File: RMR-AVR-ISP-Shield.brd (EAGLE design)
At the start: 68.6 x 53.3 mm, 31 parts, among them IC1 AVR-MEGA-PZIF_SOCKET, J1 AVR_SPI_PRG_6PTH, U1 ARDUINO_SHIELDLABEL, X1 16.00MHz, Y1 16MHz

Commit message: Add files via upload
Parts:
- added C4: 10uF, SparkFun-Capacitors:CPOL-RADIAL-2.5MM-5MM
- moved SW2 10.2 mm to (17.8, 2.54), turned to 0 degrees
- moved R3 5.08 mm to (47.0, 34.3)
- moved R4 2.54 mm to (47.0, 39.4)
- moved R5 2.54 mm to (47.0, 36.8)
- moved JP1 1.80 mm to (0.00, 8.89)
- moved LED1 1.27 mm to (31.8, 36.8)
- moved LED2 1.27 mm to (31.8, 44.5)
- moved LED3 1.27 mm to (19.1, 36.8)
- moved LED4 1.27 mm to (19.1, 44.5)
- turned R6 to 270 degrees
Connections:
- net GND: now also C4.2
- net RES: now also C4.1
- net RX: no longer IC1.3
- net TX: no longer IC1.2
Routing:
- net MISO: track 20.2 -> 74.1 mm
- net MOSI: track 21.7 -> 65.0 mm
- net SCK: track 23.5 -> 64.4 mm
- net SLV_RST: track 62.8 -> 96.0 mm
- net RES: track 25.2 -> 35.4 mm
- net N$6: track 45.4 -> 35.9 mm
- net XTAL1: track 13.8 -> 18.1 mm
- net N$1: track 11.0 -> 7.85 mm
- net TX: track 0.00 -> 2.54 mm
- net RX: track 0.00 -> 2.54 mm
- net VCC: track 115.4 -> 117.5 mm
- net N$5: track 15.5 -> 13.8 mm
- net N$4: track 12.0 -> 10.7 mm
- net N$2: track 12.0 -> 10.7 mm
- net D9: track 12.3 -> 13.5 mm
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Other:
- board text added: "PROG"
- board text removed: "8/24/21"
- board text removed: "PROGRAM"

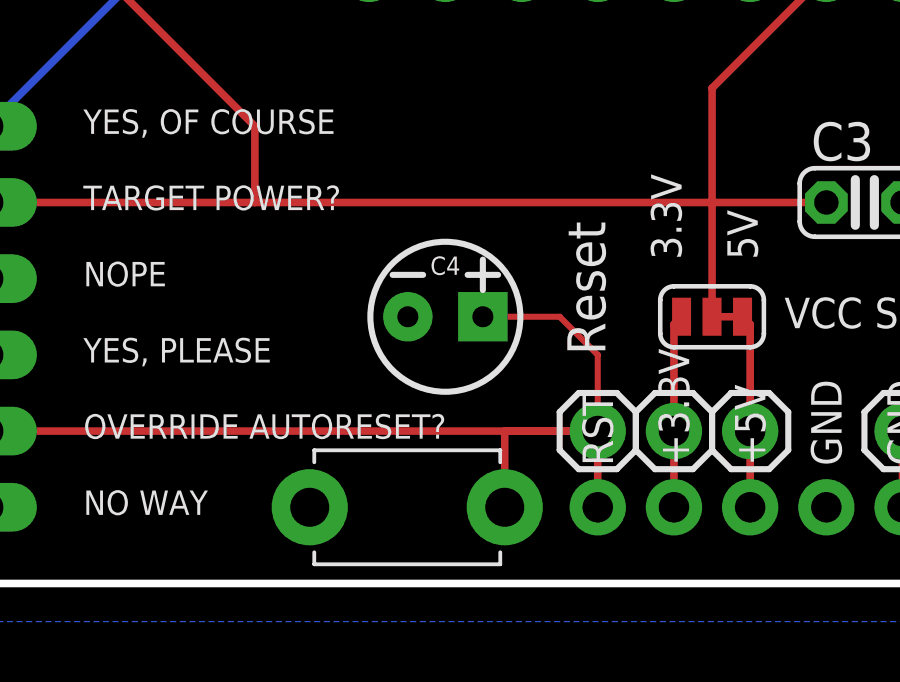
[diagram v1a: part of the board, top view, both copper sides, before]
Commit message: Add files via upload
changed reset capacitor
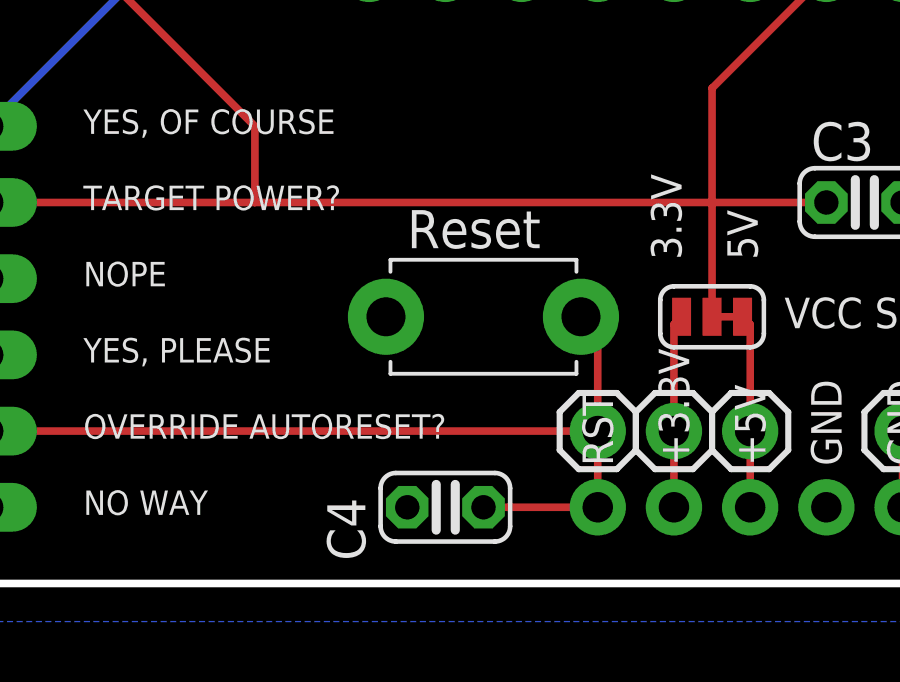
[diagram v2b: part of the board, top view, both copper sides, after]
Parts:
- C4: value 10uF -> 0.1uF; device SparkFun-Capacitors:CPOL-RADIAL-2.5MM-5MM -> adafruit:C025-024X044
- moved SW2 6.84 mm to (20.3, 8.89)
- moved C4 6.35 mm to (19.1, 2.54)
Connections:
- net GND: now also C4.1; no longer C4.2
- net RES: now also C4.2; no longer C4.1
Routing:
- net RES: track 35.4 -> 30.7 mm
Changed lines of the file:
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@@
 <text x="6.985" y="14.986" size="0.8128" layer="21" font="vector" ratio="15">YES, OF COURSE</text>
 <text x="29.464" y="10.795" size="1.016" layer="21" font="vector" ratio="15" rot="R90">5V</text>
-<text x="24.384" y="7.62" size="1.27" layer="21" font="vector" ratio="15" rot="R90">Reset</text>
+<text x="17.78" y="11.176" size="1.27" layer="21" font="vector" ratio="15">Reset</text>
 <text x="52.07" y="23.749" size="1.778" layer="22" font="vector" ratio="15" rot="MR0">RabbitMountainResearch.com</text>
 </plain>
@@
 <attribute name="VALUE" x="53.34" y="46.736" size="0.6096" layer="27" font="vector" ratio="20" align="top-left"/>
 </element>
-<element name="SW2" library="adafruit" library_urn="urn:adsk.eagle:library:420" package="TACT_PANA-EVQ" package3d_urn="urn:adsk.eagle:package:6240957/1" value="" x="17.78" y="2.54" smashed="yes">
-<attribute name="VALUE" x="14.764" y="0.089" size="0.4064" layer="27" ratio="10"/>
-</element>
-<element name="C4" library="SparkFun-Capacitors" library_urn="urn:adsk.eagle:library:510" package="CPOL-RADIAL-2.5MM-5MM" package3d_urn="urn:adsk.eagle:package:37423/1" value="10uF" x="19.05" y="8.89" smashed="yes">
-<attribute name="NAME" x="19.05" y="10.287" size="0.6096" layer="25" font="vector" ratio="20" align="bottom-center"/>
-<attribute name="PROD_ID" value="CAP-08440" x="19.05" y="8.89" size="1.778" layer="27" display="off"/>
-<attribute name="VALUE" x="19.05" y="7.493" size="0.6096" layer="27" font="vector" ratio="20" align="top-center"/>
+<element name="SW2" library="adafruit" library_urn="urn:adsk.eagle:library:420" package="TACT_PANA-EVQ" package3d_urn="urn:adsk.eagle:package:6240957/1" value="" x="20.32" y="8.89" smashed="yes">
+<attribute name="VALUE" x="17.304" y="6.439" size="0.4064" layer="27" ratio="10"/>
+</element>
+<element name="C4" library="adafruit" library_urn="urn:adsk.eagle:library:420" package="C025-024X044" package3d_urn="urn:adsk.eagle:package:6240324/1" value="0.1uF" x="19.05" y="2.54" smashed="yes">
+<attribute name="NAME" x="16.383" y="0.762" size="1.27" layer="25" ratio="10" rot="R90"/>
 </element>
 </elements>
@@
 <vertex x="-10.16" y="54.61"/>
 </polygon>
-<contactref element="C4" pad="2"/>
+<contactref element="C4" pad="1"/>
 </signal>
 <signal name="5V">
@@
 <contactref element="SW2" pad="P$2"/>
 <wire x1="24.13" y1="2.54" x2="24.13" y2="5.08" width="0.254" layer="1"/>
-<wire x1="24.13" y1="5.08" x2="21.03" y2="5.08" width="0.254" layer="1"/>
-<wire x1="21.03" y1="5.08" x2="21.03" y2="2.54" width="0.254" layer="1"/>
 <wire x1="3.81" y1="5.08" x2="24.13" y2="5.08" width="0.254" layer="1"/>
-<contactref element="C4" pad="1"/>
-<wire x1="20.3" y1="8.89" x2="22.86" y2="8.89" width="0.2032" layer="1"/>
-<wire x1="24.13" y1="7.62" x2="22.86" y2="8.89" width="0.2032" layer="1"/>
-<wire x1="24.13" y1="7.62" x2="24.13" y2="5.08" width="0.2032" layer="1"/>
+<contactref element="C4" pad="2"/>
+<wire x1="23.57" y1="8.89" x2="24.13" y2="8.33" width="0.254" layer="1"/>
+<wire x1="24.13" y1="8.33" x2="24.13" y2="5.08" width="0.254" layer="1"/>
+<wire x1="20.32" y1="2.54" x2="24.13" y2="2.54" width="0.254" layer="1"/>
 </signal>
 <signal name="VCC">

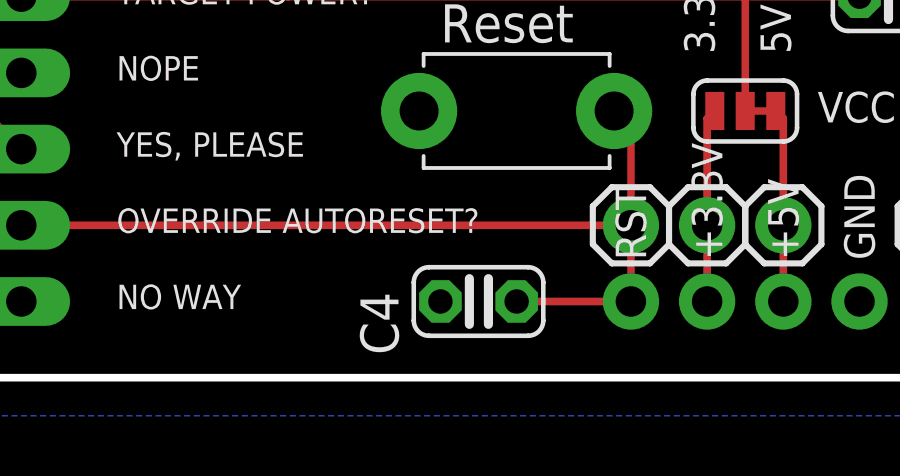
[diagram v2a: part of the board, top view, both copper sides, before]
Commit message: Add files via upload
added jumper to the reset capacitor for UNO / 328p based Arduinos.
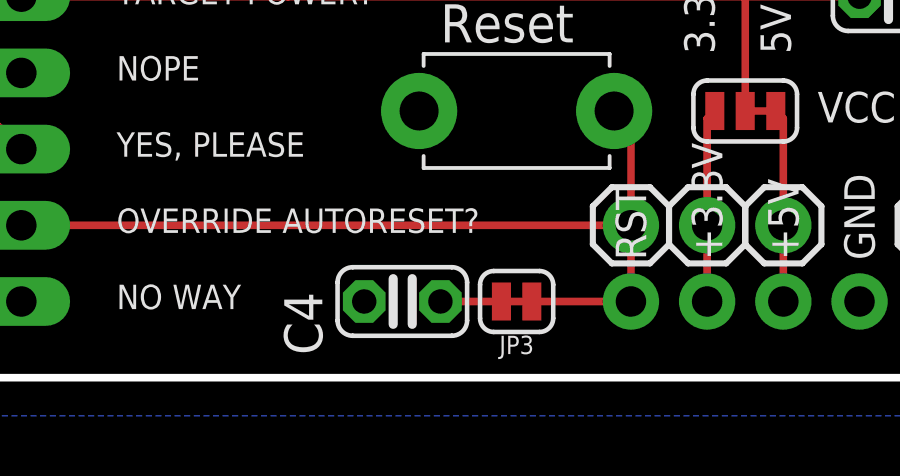
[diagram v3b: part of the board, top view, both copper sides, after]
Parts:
- added JP3: JUMPER-SMT_2_NC_TRACE_SILK, SparkFun-Jumpers:SMT-JUMPER_2_NC_TRACE_SILK
- moved C4 2.54 mm to (16.5, 2.54)
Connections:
- new net N$7: C4.2, JP3.1
- net RES: now also JP3.2; no longer C4.2
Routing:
- net N$7: track 0.00 -> 2.03 mm
- net RES: track 30.7 -> 30.2 mm
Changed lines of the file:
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@@
 <attribute name="VALUE" x="17.304" y="6.439" size="0.4064" layer="27" ratio="10"/>
 </element>
-<element name="C4" library="adafruit" library_urn="urn:adsk.eagle:library:420" package="C025-024X044" package3d_urn="urn:adsk.eagle:package:6240324/1" value="0.1uF" x="19.05" y="2.54" smashed="yes">
-<attribute name="NAME" x="16.383" y="0.762" size="1.27" layer="25" ratio="10" rot="R90"/>
+<element name="C4" library="adafruit" library_urn="urn:adsk.eagle:library:420" package="C025-024X044" package3d_urn="urn:adsk.eagle:package:6240324/1" value="0.1uF" x="16.51" y="2.54" smashed="yes">
+<attribute name="NAME" x="13.843" y="0.762" size="1.27" layer="25" ratio="10" rot="R90"/>
+</element>
+<element name="JP3" library="SparkFun-Jumpers" library_urn="urn:adsk.eagle:library:528" package="SMT-JUMPER_2_NC_TRACE_SILK" package3d_urn="urn:adsk.eagle:package:39281/1" value="JUMPER-SMT_2_NC_TRACE_SILK" x="20.32" y="2.54" smashed="yes">
+<attribute name="NAME" x="20.32" y="1.397" size="0.6096" layer="25" font="vector" ratio="20" rot="R180" align="bottom-center"/>
 </element>
 </elements>
@@
 <wire x1="24.13" y1="2.54" x2="24.13" y2="5.08" width="0.254" layer="1"/>
 <wire x1="3.81" y1="5.08" x2="24.13" y2="5.08" width="0.254" layer="1"/>
-<contactref element="C4" pad="2"/>
 <wire x1="23.57" y1="8.89" x2="24.13" y2="8.33" width="0.254" layer="1"/>
 <wire x1="24.13" y1="8.33" x2="24.13" y2="5.08" width="0.254" layer="1"/>
-<wire x1="20.32" y1="2.54" x2="24.13" y2="2.54" width="0.254" layer="1"/>
+<contactref element="JP3" pad="2"/>
+<wire x1="20.828" y1="2.54" x2="24.13" y2="2.54" width="0.254" layer="1"/>
 </signal>
 <signal name="VCC">
@@
 <wire x1="6.35" y1="46.99" x2="10.16" y2="43.18" width="0.254" layer="16"/>
 </signal>
+<signal name="N$7">
+<contactref element="C4" pad="2"/>
+<contactref element="JP3" pad="1"/>
+<wire x1="19.812" y1="2.54" x2="17.78" y2="2.54" width="0.254" layer="1"/>
+</signal>
 </signals>
